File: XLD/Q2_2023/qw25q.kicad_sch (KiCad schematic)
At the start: 521 parts

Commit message: various fixes
swap L3-20 with L2-17 in qblox
change ip of Lo18 to 192.168.0.208 (tii1q_b4 twpa pump) and type to ERA
rename LO_ERA_pp to LO_ERA
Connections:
- net at EF43.: now also LPF34.; no longer L:96.
- net at EF52.: now also LPF43.; no longer L:104.
- net at EF29.: now also L:5.; no longer LPF20.
- net at EF69.: now also L:153.; no longer LPF60.
- net at Coupler1.: now also L:3.; no longer L:4. (x2)
- net at L:3.: now also TWPA1.; no longer Coupler1.
- net at EF39.: now also LPF30.; no longer L:92.
- net at L:4.: now also Coupler1.; no longer TJI2. (x2)
- net at EF71.: now also LPF62.; no longer L:170.
- net at EF50.: now also L:102.; no longer LPF41.
- net at EF46.: now also L:98.; no longer LPF37.
- net at EF54.: now also L:106.; no longer LPF45.
- net at TJI2.: now also L:4.; no longer L:5.
- net at TWPA1.: now also L:3.; no longer L:2. (x2)
- net at L:3.: now also Coupler1.; no longer TWPA1. (x2)
- net at EF37.: now also L:27.; no longer LPF28.
- net at L:1.: now also TJI1.
- net at TJI1.: now also L:2.; no longer L:1.
- net at L:2.: now also TJI1.; no longer TWPA1. (x2)
- net at TJI1.: now also L:1.; no longer L:2. (x2)
- net at EF70.: now also L:168.; no longer LPF61.
- net at EF33.: now also LPF24.; no longer L:9.
- net at EF31.: now also LPF22.; no longer L:7.
- net at EF64.: now also LPF55.; no longer L:116.
- net at EF27.: now also L:3.; no longer LPF18.
- net at EF62.: now also L:114.; no longer LPF53.
- net at EF68.: now also L:120.; no longer LPF59.
- net at EF66.: now also LPF57.; no longer L:118.
- net at EF41.: now also LPF32.; no longer L:94.
- net at L:4.: now also TJI2.; no longer Coupler1.
- net at EF72.: now also L:174.; no longer LPF63.
- net at L:2.: now also TWPA1.; no longer TJI1.
- net at EF56.: now also L:108.; no longer LPF47.
- net at TJI2.: now also L:5.; no longer L:4.
- net at EF35.: now also L:25.; no longer LPF26.
- net at EF48.: now also L:100.; no longer LPF39.
- net at EF60.: now also LPF51.; no longer L:112.
- net at EF58.: now also LPF49.; no longer L:110.
- new net: EF43., L:96.
- new net: EF52., L:104.
- new net: EF29., LPF20.
- new net: ATT347., ATT348.
- new net: EF69., LPF60.
- new net: Coupler1., L:4. (x2)
- new net: EF39., L:92.
- new net: EF44., LPF35.
- new net: L:4., TJI2.
- new net: EF55., LPF46.
- new net: EF71., L:170.
- new net: EF38., LPF29.
- new net: EF50., LPF41.
- new net: EF46., LPF37.
- new net: EF47., LPF38.
- new net: ATT351., ATT352.
- new net: EF54., LPF45.
- new net: L:5., TJI2.
- new net: L:2., TWPA1. (x3)
- new net: EF37., LPF28.
- new net: EF51., LPF42.
- new net: EF70., LPF61.
- new net: ATT349., ATT350.
- new net: ATT345., ATT346.
- new net: EF65., LPF56.
- new net: EF33., L:9.
- new net: L:6., LX-X2. (x3)
- new net: EF31., L:7.
- new net: EF30., LPF21.
- new net: EF64., L:116.
- new net: EF57., LPF48.
- new net: EF27., LPF18.
- new net: EF49., LPF40.
- new net: EF61., LPF52.
- new net: EF62., LPF53.
- new net: EF68., LPF59.
- new net: EF66., L:118.
- new net: EF41., L:94.
- new net: EF72., LPF63.
- new net: L:2., TJI1.
- new net: EF40., LPF31.
- new net: EF28., LPF19.
- new net: EF56., LPF47.
- new net: EF67., LPF58.
- new net: EF35., LPF26.
- new net: EF63., LPF54.
- new net: EF36., LPF27.
- new net: EF45., LPF36.
- new net: EF53., LPF44.
- new net: EF48., LPF39.
- new net: EF60., L:112.
- new net: EF32., LPF23.
- new net: EF58., L:110.
- new net: EF42., LPF33.
- new net: EF34., LPF25.
- new net: EF59., LPF50.

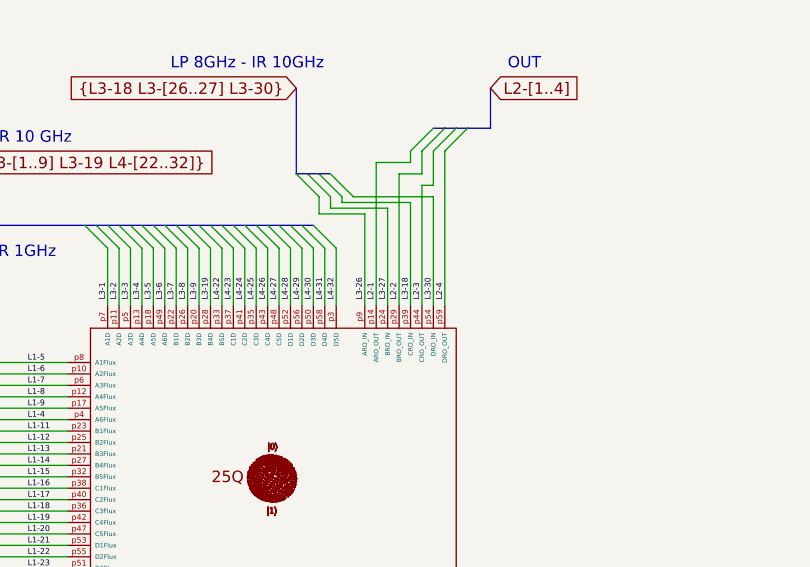
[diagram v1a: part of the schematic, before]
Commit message: corrected the output lines for the readout for QW25q
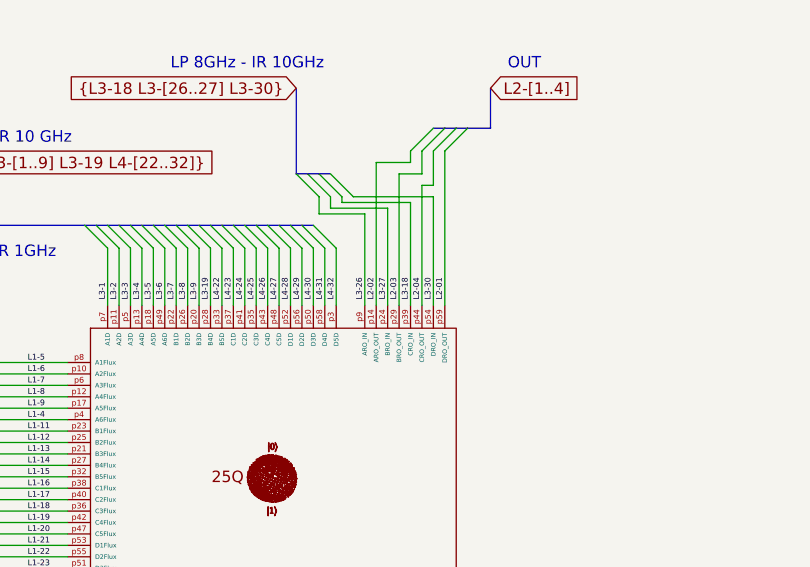
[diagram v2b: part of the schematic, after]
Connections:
- net L2-1: no longer QPU?.p14 (ARO_OUT)
- net L2-2: no longer QPU?.p29 (BRO_OUT)
- net L2-3: no longer QPU?.p44 (CRO_OUT)
- net L2-4: no longer QPU?.p59 (DRO_OUT)
- net at EF43.: now also LPF34.; no longer L:96.
- net at EF52.: now also LPF43.; no longer L:104.
- net at EF29.: now also L:5.; no longer LPF20.
- net at EF69.: now also L:153.; no longer LPF60.
- net at Coupler1.: now also L:3.; no longer L:4. (x2)
- net at L:3.: now also TWPA1.; no longer Coupler1.
- net at EF39.: now also LPF30.; no longer L:92.
- net at L:4.: now also Coupler1.; no longer TJI2. (x2)
- net at EF71.: now also LPF62.; no longer L:170.
- net at EF50.: now also L:102.; no longer LPF41.
- net at EF46.: now also L:98.; no longer LPF37.
- net at EF54.: now also L:106.; no longer LPF45.
- net at TJI2.: now also L:4.; no longer L:5.
- net at TWPA1.: now also L:3.; no longer L:2. (x2)
- net at L:3.: now also Coupler1.; no longer TWPA1. (x2)
- net at EF37.: now also L:27.; no longer LPF28.
- net at L:1.: now also TJI1.
- net at TJI1.: now also L:2.; no longer L:1.
- net at L:2.: now also TJI1.; no longer TWPA1. (x2)
- net at TJI1.: now also L:1.; no longer L:2. (x2)
- net at EF70.: now also L:168.; no longer LPF61.
- net at EF33.: now also LPF24.; no longer L:9.
- net at EF31.: now also LPF22.; no longer L:7.
- net at EF64.: now also LPF55.; no longer L:116.
- net at EF27.: now also L:3.; no longer LPF18.
- net at EF62.: now also L:114.; no longer LPF53.
- net at EF68.: now also L:120.; no longer LPF59.
- net at EF66.: now also LPF57.; no longer L:118.
- net at EF41.: now also LPF32.; no longer L:94.
- net at L:4.: now also TJI2.; no longer Coupler1.
- net at EF72.: now also L:174.; no longer LPF63.
- net at L:2.: now also TWPA1.; no longer TJI1.
- net at EF56.: now also L:108.; no longer LPF47.
- net at TJI2.: now also L:5.; no longer L:4.
- net at EF35.: now also L:25.; no longer LPF26.
- net at EF48.: now also L:100.; no longer LPF39.
- net at EF60.: now also LPF51.; no longer L:112.
- net at EF58.: now also LPF49.; no longer L:110.
- new net: EF43., L:96.
- new net: EF52., L:104.
- new net: EF29., LPF20.
- new net: ATT347., ATT348.
- new net: EF69., LPF60.
- new net: Coupler1., L:4. (x2)
- new net: EF39., L:92.
- new net: EF44., LPF35.
- new net: L:4., TJI2.
- new net: EF55., LPF46.
- new net: EF71., L:170.
- new net: EF38., LPF29.
- new net: EF50., LPF41.
- new net: EF46., LPF37.
- new net: EF47., LPF38.
- new net: ATT351., ATT352.
- new net: EF54., LPF45.
- new net: L:5., TJI2.
- new net: L:2., TWPA1. (x3)
- new net: EF37., LPF28.
- new net: EF51., LPF42.
- new net: EF70., LPF61.
- new net: ATT349., ATT350.
- new net: ATT345., ATT346.
- new net: EF65., LPF56.
- new net: EF33., L:9.
- new net: L:6., LX-X2. (x3)
- new net: EF31., L:7.
- new net: EF30., LPF21.
- new net: EF64., L:116.
- new net: EF57., LPF48.
- new net: EF27., LPF18.
- new net: EF49., LPF40.
- new net: EF61., LPF52.
- new net: EF62., LPF53.
- new net: EF68., LPF59.
- new net: EF66., L:118.
- new net: EF41., L:94.
- new net: EF72., LPF63.
- new net: L:2., TJI1.
- new net: EF40., LPF31.
- new net: EF28., LPF19.
- new net: EF56., LPF47.
- new net: EF67., LPF58.
- new net: EF35., LPF26.
- new net: EF63., LPF54.
- new net: EF36., LPF27.
- new net: EF45., LPF36.
- new net: EF53., LPF44.
- new net: EF48., LPF39.
- new net: EF60., L:112.
- new net: EF32., LPF23.
- new net: EF58., L:110.
- new net: EF42., LPF33.
- new net: EF34., LPF25.
- new net: EF59., LPF50.
- new net L2-01: QPU?.p59 (DRO_OUT)
- new net L2-02: QPU?.p14 (ARO_OUT)
- new net L2-03: QPU?.p29 (BRO_OUT)
- new net L2-04: QPU?.p44 (CRO_OUT)
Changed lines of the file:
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@@
     (effects (font (size 1.27 1.27)) (justify left bottom))
   )
-  (label "L2-4" (at 681.355 448.31 90) (fields_autoplaced)
+  (label "L2-01" (at 681.355 448.31 90) (fields_autoplaced)
     (effects (font (size 0.64 0.64)) (justify left bottom))
   )
@@
     (effects (font (size 1.27 1.27)) (justify left bottom))
   )
-  (label "L2-1" (at 673.735 448.31 90) (fields_autoplaced)
+  (label "L2-02" (at 673.735 448.31 90) (fields_autoplaced)
     (effects (font (size 0.64 0.64)) (justify left bottom))
   )
@@
     (effects (font (size 1.27 1.27)) (justify left bottom))
   )
-  (label "L2-2" (at 676.275 448.31 90) (fields_autoplaced)
+  (label "L2-03" (at 676.275 448.31 90) (fields_autoplaced)
     (effects (font (size 0.64 0.64)) (justify left bottom))
   )
@@
     (effects (font (size 1.27 1.27)) (justify left bottom))
   )
-  (label "L2-3" (at 678.815 448.31 90) (fields_autoplaced)
-    (effects (font (size 0.64 0.64)) (justify left bottom))
-  )
+  (label "L2-04" (at 678.815 448.31 90) (fields_autoplaced)
+    (effects (font (size 0.64 0.64)) (justify left bottom))
+  )

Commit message: added changes of filter thermalization for flux lines qw25q
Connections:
- net at EF43.: now also LPF34.; no longer L:96.
- net at EF52.: now also LPF43.; no longer L:104.
- net at EF29.: now also L:5.; no longer LPF20.
- net at EF69.: now also L:153.; no longer LPF60.
- net at Coupler1.: now also L:3.; no longer L:4. (x2)
- net at L:3.: now also TWPA1.; no longer Coupler1.
- net at EF39.: now also LPF30.; no longer L:92.
- net at L:4.: now also Coupler1.; no longer TJI2. (x2)
- net at EF71.: now also LPF62.; no longer L:170.
- net at EF50.: now also L:102.; no longer LPF41.
- net at EF46.: now also L:98.; no longer LPF37.
- net at EF54.: now also L:106.; no longer LPF45.
- net at TJI2.: now also L:4.; no longer L:5.
- net at TWPA1.: now also L:3.; no longer L:2. (x2)
- net at L:3.: now also Coupler1.; no longer TWPA1. (x2)
- net at EF37.: now also L:27.; no longer LPF28.
- net at L:1.: now also TJI1.
- net at TJI1.: now also L:2.; no longer L:1.
- net at L:2.: now also TJI1.; no longer TWPA1. (x2)
- net at TJI1.: now also L:1.; no longer L:2. (x2)
- net at EF70.: now also L:168.; no longer LPF61.
- net at EF33.: now also LPF24.; no longer L:9.
- net at EF31.: now also LPF22.; no longer L:7.
- net at EF64.: now also LPF55.; no longer L:116.
- net at EF27.: now also L:3.; no longer LPF18.
- net at EF62.: now also L:114.; no longer LPF53.
- net at EF68.: now also L:120.; no longer LPF59.
- net at EF66.: now also LPF57.; no longer L:118.
- net at EF41.: now also LPF32.; no longer L:94.
- net at L:4.: now also TJI2.; no longer Coupler1.
- net at EF72.: now also L:174.; no longer LPF63.
- net at L:2.: now also TWPA1.; no longer TJI1.
- net at EF56.: now also L:108.; no longer LPF47.
- net at TJI2.: now also L:5.; no longer L:4.
- net at EF35.: now also L:25.; no longer LPF26.
- net at EF48.: now also L:100.; no longer LPF39.
- net at EF60.: now also LPF51.; no longer L:112.
- net at EF58.: now also LPF49.; no longer L:110.
- new net: EF43., L:96.
- new net: EF52., L:104.
- new net: EF29., LPF20.
- new net: ATT347., ATT348.
- new net: EF69., LPF60.
- new net: Coupler1., L:4. (x2)
- new net: EF39., L:92.
- new net: EF44., LPF35.
- new net: L:4., TJI2.
- new net: EF55., LPF46.
- new net: EF71., L:170.
- new net: EF38., LPF29.
- new net: EF50., LPF41.
- new net: EF46., LPF37.
- new net: EF47., LPF38.
- new net: ATT351., ATT352.
- new net: EF54., LPF45.
- new net: L:5., TJI2.
- new net: L:2., TWPA1. (x3)
- new net: EF37., LPF28.
- new net: EF51., LPF42.
- new net: EF70., LPF61.
- new net: ATT349., ATT350.
- new net: ATT345., ATT346.
- new net: EF65., LPF56.
- new net: EF33., L:9.
- new net: L:6., LX-X2. (x3)
- new net: EF31., L:7.
- new net: EF30., LPF21.
- new net: EF64., L:116.
- new net: EF57., LPF48.
- new net: EF27., LPF18.
- new net: EF49., LPF40.
- new net: EF61., LPF52.
- new net: EF62., LPF53.
- new net: EF68., LPF59.
- new net: EF66., L:118.
- new net: EF41., L:94.
- new net: EF72., LPF63.
- new net: L:2., TJI1.
- new net: EF40., LPF31.
- new net: EF28., LPF19.
- new net: EF56., LPF47.
- new net: EF67., LPF58.
- new net: EF35., LPF26.
- new net: EF63., LPF54.
- new net: EF36., LPF27.
- new net: EF45., LPF36.
- new net: EF53., LPF44.
- new net: EF48., LPF39.
- new net: EF60., L:112.
- new net: EF32., LPF23.
- new net: EF58., L:110.
- new net: EF42., LPF33.
- new net: EF34., LPF25.
- new net: EF59., LPF50.
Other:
- moved on the sheet: LPF31, LPF33, LPF35, LPF36, LPF38, LPF40, LPF42, LPF44, LPF46, LPF48, LPF50, LPF52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

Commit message: added labels to lo3 splitter exits
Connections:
- net at EF43.: now also LPF34.; no longer L:96.
- net at EF52.: now also LPF43.; no longer L:104.
- net at EF29.: now also L:5.; no longer LPF20.
- net at EF69.: now also L:153.; no longer LPF60.
- net at Coupler1.: now also L:3.; no longer L:4. (x2)
- net at L:3.: now also TWPA1.; no longer Coupler1.
- net at EF39.: now also LPF30.; no longer L:92.
- net at L:4.: now also Coupler1.; no longer TJI2. (x2)
- net at EF71.: now also LPF62.; no longer L:170.
- net at EF50.: now also L:102.; no longer LPF41.
- net at EF46.: now also L:98.; no longer LPF37.
- net at EF54.: now also L:106.; no longer LPF45.
- net at TJI2.: now also L:4.; no longer L:5.
- net at TWPA1.: now also L:3.; no longer L:2. (x2)
- net at L:3.: now also Coupler1.; no longer TWPA1. (x2)
- net at EF37.: now also L:27.; no longer LPF28.
- net at L:1.: now also TJI1.
- net at TJI1.: now also L:2.; no longer L:1.
- net at L:2.: now also TJI1.; no longer TWPA1. (x2)
- net at TJI1.: now also L:1.; no longer L:2. (x2)
- net at EF70.: now also L:168.; no longer LPF61.
- net at EF33.: now also LPF24.; no longer L:9.
- net at EF31.: now also LPF22.; no longer L:7.
- net at EF64.: now also LPF55.; no longer L:116.
- net at EF27.: now also L:3.; no longer LPF18.
- net at EF62.: now also L:114.; no longer LPF53.
- net at EF68.: now also L:120.; no longer LPF59.
- net at EF66.: now also LPF57.; no longer L:118.
- net at EF41.: now also LPF32.; no longer L:94.
- net at L:4.: now also TJI2.; no longer Coupler1.
- net at EF72.: now also L:174.; no longer LPF63.
- net at L:2.: now also TWPA1.; no longer TJI1.
- net at EF56.: now also L:108.; no longer LPF47.
- net at TJI2.: now also L:5.; no longer L:4.
- net at EF35.: now also L:25.; no longer LPF26.
- net at EF48.: now also L:100.; no longer LPF39.
- net at EF60.: now also LPF51.; no longer L:112.
- net at EF58.: now also LPF49.; no longer L:110.
- new net: EF43., L:96.
- new net: EF52., L:104.
- new net: EF29., LPF20.
- new net: ATT347., ATT348.
- new net: EF69., LPF60.
- new net: Coupler1., L:4. (x2)
- new net: EF39., L:92.
- new net: EF44., LPF35.
- new net: L:4., TJI2.
- new net: EF55., LPF46.
- new net: EF71., L:170.
- new net: EF38., LPF29.
- new net: EF50., LPF41.
- new net: EF46., LPF37.
- new net: EF47., LPF38.
- new net: ATT351., ATT352.
- new net: EF54., LPF45.
- new net: L:5., TJI2.
- new net: L:2., TWPA1. (x3)
- new net: EF37., LPF28.
- new net: EF51., LPF42.
- new net: EF70., LPF61.
- new net: ATT349., ATT350.
- new net: ATT345., ATT346.
- new net: EF65., LPF56.
- new net: EF33., L:9.
- new net: L:6., LX-X2. (x3)
- new net: EF31., L:7.
- new net: EF30., LPF21.
- new net: EF64., L:116.
- new net: EF57., LPF48.
- new net: EF27., LPF18.
- new net: EF49., LPF40.
- new net: EF61., LPF52.
- new net: EF62., LPF53.
- new net: EF68., LPF59.
- new net: EF66., L:118.
- new net: EF41., L:94.
- new net: EF72., LPF63.
- new net: L:2., TJI1.
- new net: EF40., LPF31.
- new net: EF28., LPF19.
- new net: EF56., LPF47.
- new net: EF67., LPF58.
- new net: EF35., LPF26.
- new net: EF63., LPF54.
- new net: EF36., LPF27.
- new net: EF45., LPF36.
- new net: EF53., LPF44.
- new net: EF48., LPF39.
- new net: EF60., L:112.
- new net: EF32., LPF23.
- new net: EF58., L:110.
- new net: EF42., LPF33.
- new net: EF34., LPF25.
- new net: EF59., LPF50.

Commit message: Updated the labeling for the cables from the splitters to the controller for the local oscillators 3 and 4
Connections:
- net at EF43.: now also LPF34.; no longer L:96.
- net at EF52.: now also LPF43.; no longer L:104.
- net at EF29.: now also L:5.; no longer LPF20.
- net at EF69.: now also L:153.; no longer LPF60.
- net at Coupler1.: now also L:3.; no longer L:4. (x2)
- net at L:3.: now also TWPA1.; no longer Coupler1.
- net at EF39.: now also LPF30.; no longer L:92.
- net at L:4.: now also Coupler1.; no longer TJI2. (x2)
- net at EF71.: now also LPF62.; no longer L:170.
- net at EF50.: now also L:102.; no longer LPF41.
- net at EF46.: now also L:98.; no longer LPF37.
- net at EF54.: now also L:106.; no longer LPF45.
- net at TJI2.: now also L:4.; no longer L:5.
- net at TWPA1.: now also L:3.; no longer L:2. (x2)
- net at L:3.: now also Coupler1.; no longer TWPA1. (x2)
- net at EF37.: now also L:27.; no longer LPF28.
- net at L:1.: now also TJI1.
- net at TJI1.: now also L:2.; no longer L:1.
- net at L:2.: now also TJI1.; no longer TWPA1. (x2)
- net at TJI1.: now also L:1.; no longer L:2. (x2)
- net at EF70.: now also L:168.; no longer LPF61.
- net at EF33.: now also LPF24.; no longer L:9.
- net at EF31.: now also LPF22.; no longer L:7.
- net at EF64.: now also LPF55.; no longer L:116.
- net at EF27.: now also L:3.; no longer LPF18.
- net at EF62.: now also L:114.; no longer LPF53.
- net at EF68.: now also L:120.; no longer LPF59.
- net at EF66.: now also LPF57.; no longer L:118.
- net at EF41.: now also LPF32.; no longer L:94.
- net at L:4.: now also TJI2.; no longer Coupler1.
- net at EF72.: now also L:174.; no longer LPF63.
- net at L:2.: now also TWPA1.; no longer TJI1.
- net at EF56.: now also L:108.; no longer LPF47.
- net at TJI2.: now also L:5.; no longer L:4.
- net at EF35.: now also L:25.; no longer LPF26.
- net at EF48.: now also L:100.; no longer LPF39.
- net at EF60.: now also LPF51.; no longer L:112.
- net at EF58.: now also LPF49.; no longer L:110.
- new net: EF43., L:96.
- new net: EF52., L:104.
- new net: EF29., LPF20.
- new net: ATT347., ATT348.
- new net: EF69., LPF60.
- new net: Coupler1., L:4. (x2)
- new net: EF39., L:92.
- new net: EF44., LPF35.
- new net: L:4., TJI2.
- new net: EF55., LPF46.
- new net: EF71., L:170.
- new net: EF38., LPF29.
- new net: EF50., LPF41.
- new net: EF46., LPF37.
- new net: EF47., LPF38.
- new net: ATT351., ATT352.
- new net: EF54., LPF45.
- new net: L:5., TJI2.
- new net: L:2., TWPA1. (x3)
- new net: EF37., LPF28.
- new net: EF51., LPF42.
- new net: EF70., LPF61.
- new net: ATT349., ATT350.
- new net: ATT345., ATT346.
- new net: EF65., LPF56.
- new net: EF33., L:9.
- new net: L:6., LX-X2. (x3)
- new net: EF31., L:7.
- new net: EF30., LPF21.
- new net: EF64., L:116.
- new net: EF57., LPF48.
- new net: EF27., LPF18.
- new net: EF49., LPF40.
- new net: EF61., LPF52.
- new net: EF62., LPF53.
- new net: EF68., LPF59.
- new net: EF66., L:118.
- new net: EF41., L:94.
- new net: EF72., LPF63.
- new net: L:2., TJI1.
- new net: EF40., LPF31.
- new net: EF28., LPF19.
- new net: EF56., LPF47.
- new net: EF67., LPF58.
- new net: EF35., LPF26.
- new net: EF63., LPF54.
- new net: EF36., LPF27.
- new net: EF45., LPF36.
- new net: EF53., LPF44.
- new net: EF48., LPF39.
- new net: EF60., L:112.
- new net: EF32., LPF23.
- new net: EF58., L:110.
- new net: EF42., LPF33.
- new net: EF34., LPF25.
- new net: EF59., LPF50.
